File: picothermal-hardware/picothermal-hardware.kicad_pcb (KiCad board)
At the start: 4 copper layers, 50 x 30 mm, 121 parts, among them J1 TC2030-CTX, J2 USB-C Plug, SW1 SW_Push, SW2 SW_Push, U1 W25Q16JV, U2 AP7330-W5-7, U3 AP7330-W5-7, U4 RP2040, U5 TLV62569A, U6 TLV62569A, U7 Flir LEPTON, Y1 ECS-2520MV-250-CL, Y2 12MHz

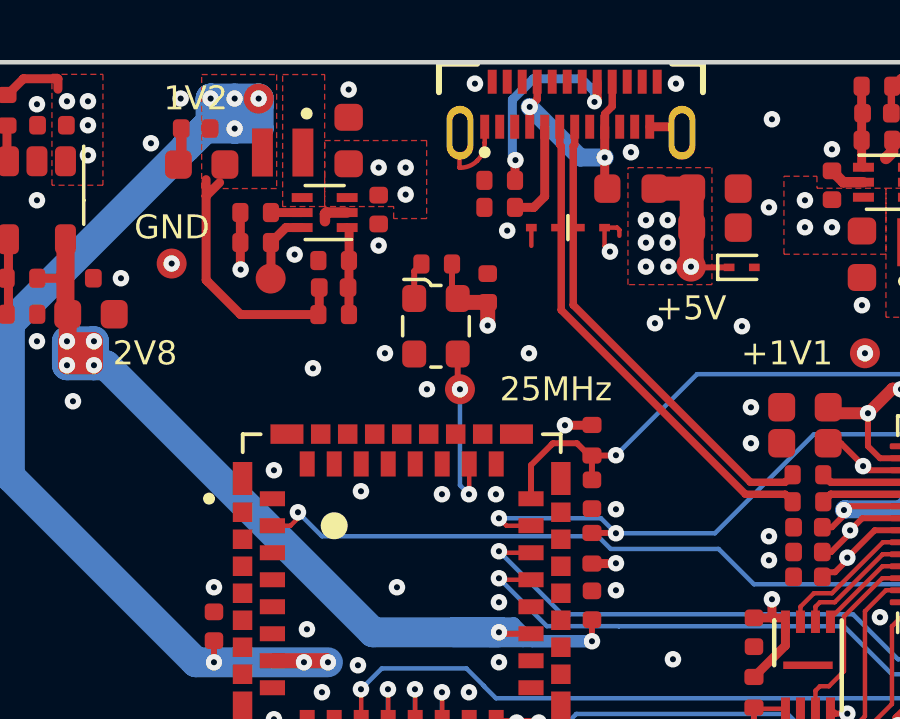
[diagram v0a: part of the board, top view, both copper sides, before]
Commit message: Updated hardware project to work with Kicad 7.0
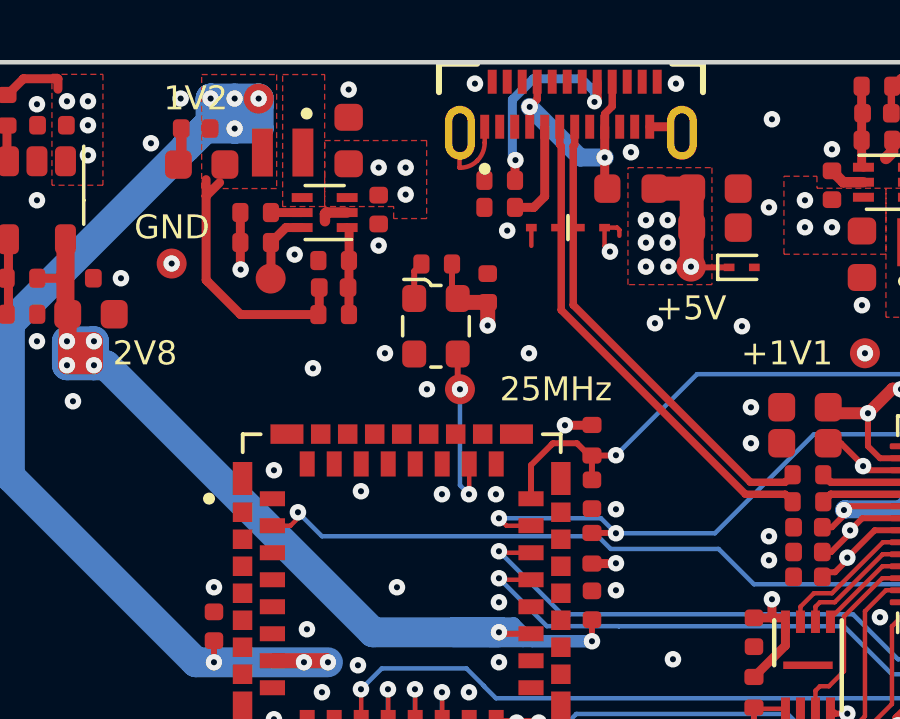
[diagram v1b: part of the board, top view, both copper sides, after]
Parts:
- R27: value 453K -> 402k
